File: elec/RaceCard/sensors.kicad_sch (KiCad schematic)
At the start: 0 parts

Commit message: + lib C3I_A25 et IQS7222A001QFR
ajout de IQS7222A001QFR dans le sch de sensors
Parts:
- added C1, C3, C5: 100pF, Capacitor_SMD:C_0603_1608Metric, symbol Device:C_Small
- added C2, C4: 2.2uF, Capacitor_SMD:C_0603_1608Metric, symbol Device:C_Small
- added C6: 4.7uF, Capacitor_SMD:C_0603_1608Metric, symbol Device:C_Small
- added U1: ~, symbol C3I_A25:IQS7222A001QFR
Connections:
- new net: C1.1, C2.1, U1.4 (VREGA)
- new net: C3.1, C4.1, U1.2 (VREGD)
- new net: C5.1, C6.1, U1.1 (VDD)
- new net GND: C1.2, C2.2, C3.2, C4.2, C5.2, C6.2, U1.21 (GND_TAB), U1.3 (VSS)

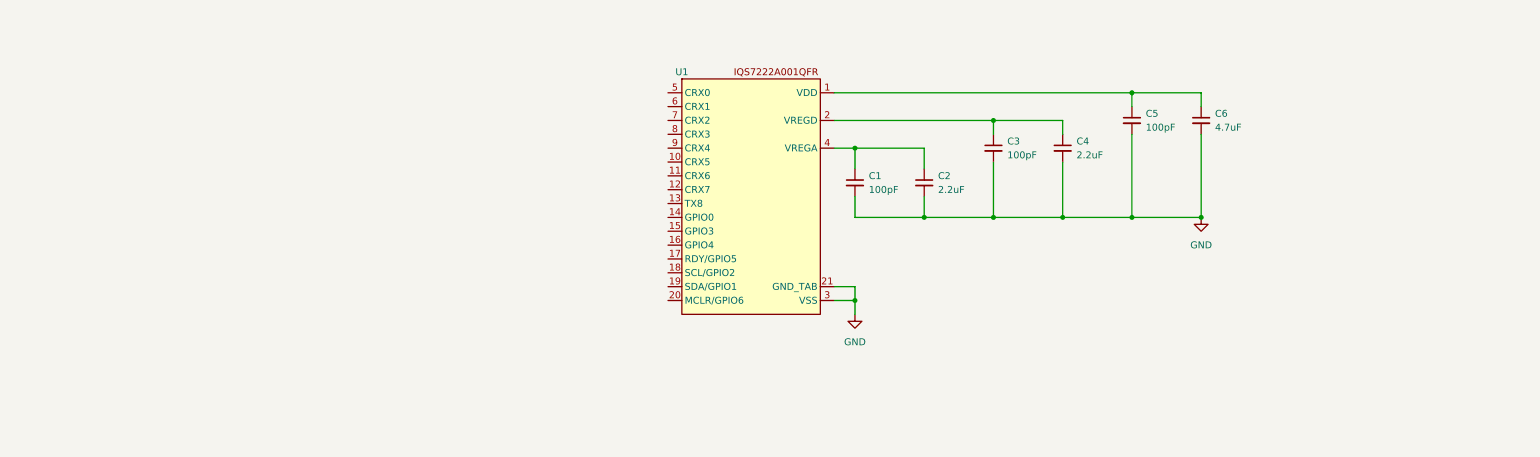
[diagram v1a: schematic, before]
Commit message: schematic slider + btns (à valider)
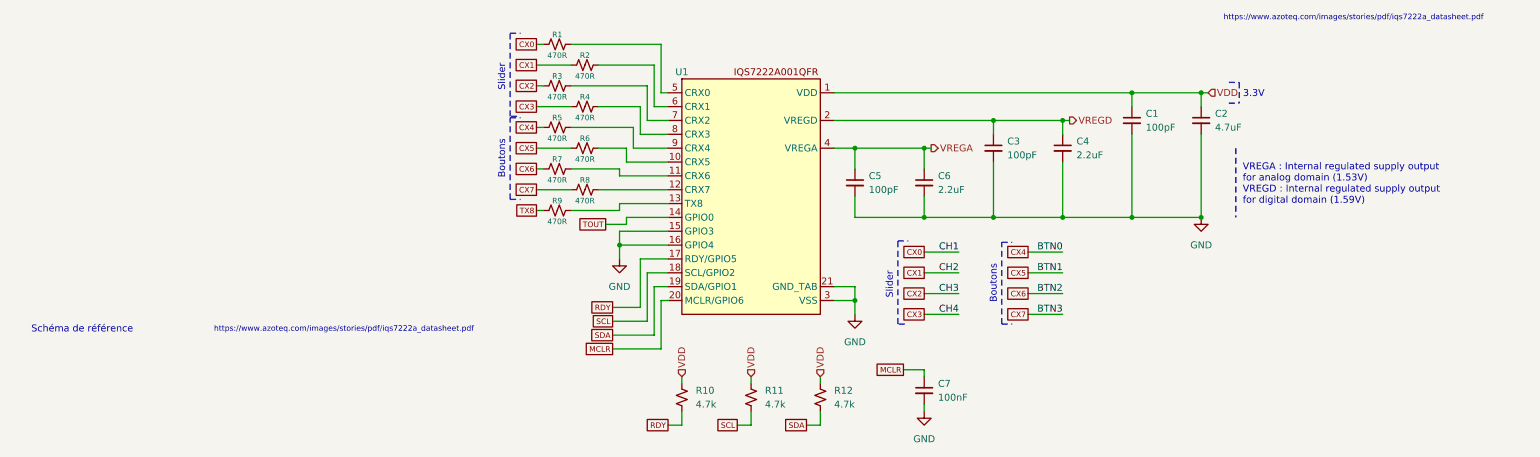
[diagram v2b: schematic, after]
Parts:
- added C7: 100nF, Capacitor_SMD:C_0603_1608Metric, symbol Device:C_Small
- added R1, R2, R3, R4, R5, R6, R7, R8, R9: 470R, Resistor_SMD:R_0603_1608Metric, symbol Device:R_Small_US
- added R10, R11, R12: 4.7k, Resistor_SMD:R_0603_1608Metric, symbol Device:R_Small_US
- U1: value ~ -> IQS7222A001QFR
- renumbered C5 to C1, C6 to C2, C1 to C5, C2 to C6
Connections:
- net GND: now also U1.15 (GPIO3), U1.16 (GPIO4), C7.2
- net VREGA: now reaches C5.1, C6.1, U1.4 (VREGA)
- net VREGD: now reaches C3.1, C4.1, U1.2 (VREGD)
- net VDD: now reaches C1.1, C2.1, U1.1 (VDD)
- net VDD: now also R10.1, R11.1, R12.1
- net at U1.10 (CRX5): now also R6.2
- net at U1.11 (CRX6): now also R7.2
- net at U1.12 (CRX7): now also R8.2
- net at U1.13 (TX8): now also R9.2
- net TOUT: now reaches U1.14 (GPIO0)
- net RDY: now reaches U1.17 (RDY/GPIO5)
- net RDY: now also R10.2
- net SCL: now reaches U1.18 (SCL/GPIO2)
- net SCL: now also R11.2
- net SDA: now reaches U1.19 (SDA/GPIO1)
- net SDA: now also R12.2
- net MCLR: now reaches U1.20 (MCLR/GPIO6)
- net MCLR: now also C7.1
- net at U1.5 (CRX0): now also R1.2
- net at U1.6 (CRX1): now also R2.2
- net at U1.7 (CRX2): now also R3.2
- net at U1.8 (CRX3): now also R4.2
- net at U1.9 (CRX4): now also R5.2
- new net CX0: R1.1
- new net CX1: R2.1
- new net CX2: R3.1
- new net CX3: R4.1
- new net CX4: R5.1
- new net CX5: R6.1
- new net CX6: R7.1
- new net CX7: R8.1
- new net TX8: R9.1
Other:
- note added: "3.3V"
- note added: "Boutons"
- note added: "Schéma de référence"
- note added: "Slider"
- note added: "VREGA : Internal regulated supply output for analog domain (1.53V) VREGD : Internal regulated supply output for digital domain (1.59V)"
- note added: "https://www.azoteq.com/images/stories/pdf/iqs7222a_datasheet.pdf"

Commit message: + test points
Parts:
- added TP2: VDD, TestPoint:TestPoint_THTPad_3.0x3.0mm_Drill1.5mm, symbol Connector:TestPoint
- renumbered C3 to C10, C4 to C11, C5 to C12, C6 to C13, C7 to C14, C1 to C8, C2 to C9, R9 to R10, R10 to R11, R11 to R12, R12 to R13, R1 to R2, R2 to R3, R3 to R4, R4 to R5, R5 to R6, R6 to R7, R7 to R8, R8 to R9, U1 to U2
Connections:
- net VDD: now also TP2.1
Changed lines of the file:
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@@
 		)
 	)
+	(wire
+		(pts
+			(xy 215.9 77.47) (xy 215.9 78.74)
+		)
+		(stroke
+			(width 0)
+			(type default)
+		)
+	)
 	(polyline
 		(pts
@@
 		(on_board yes)
 		(dnp no)
-		(property "Reference" "R6"
+		(property "Reference" "R7"
 			(at 115.57 87.122 90)
 			(effects
@@
 			(project "RaceCard"
 				(path "/fef6ab1d-cc84-41bb-aff7-8da28fd37bf7/e67e86ec-ba20-42a7-8035-4d69feadf404"
-					(reference "R6")
+					(reference "R7")
 					(unit 1)
 				)
@@
 		(dnp no)
 		(fields_autoplaced yes)
-		(property "Reference" "C5"
+		(property "Reference" "C12"
 			(at 167.64 93.9862 0)
 			(effects
@@
 			(project ""
 				(path "/fef6ab1d-cc84-41bb-aff7-8da28fd37bf7/e67e86ec-ba20-42a7-8035-4d69feadf404"
-					(reference "C5")
+					(reference "C12")
 					(unit 1)
 				)
@@
 		(dnp no)
 		(fields_autoplaced yes)
-		(property "Reference" "C4"
+		(property "Reference" "C11"
 			(at 205.74 87.6362 0)
 			(effects
@@
 			(project "RaceCard"
 				(path "/fef6ab1d-cc84-41bb-aff7-8da28fd37bf7/e67e86ec-ba20-42a7-8035-4d69feadf404"
-					(reference "C4")
+					(reference "C11")
 					(unit 1)
 				)
@@
 		(dnp no)
 		(fields_autoplaced yes)
-		(property "Reference" "C1"
+		(property "Reference" "C8"
 			(at 218.44 82.5562 0)
 			(effects
@@
 			(project "RaceCard"
 				(path "/fef6ab1d-cc84-41bb-aff7-8da28fd37bf7/e67e86ec-ba20-42a7-8035-4d69feadf404"
-					(reference "C1")
+					(reference "C8")
 					(unit 1)
 				)
@@
 		(on_board yes)
 		(dnp no)
-		(property "Reference" "R3"
+		(property "Reference" "R4"
 			(at 110.49 75.692 90)
 			(effects
@@
 			(project "RaceCard"
 				(path "/fef6ab1d-cc84-41bb-aff7-8da28fd37bf7/e67e86ec-ba20-42a7-8035-4d69feadf404"
-					(reference "R3")
+					(reference "R4")
 					(unit 1)
 				)
@@
 		(dnp no)
 		(fields_autoplaced yes)
-		(property "Reference" "R11"
+		(property "Reference" "R12"
 			(at 148.59 133.3499 0)
 			(effects
@@
 			(project "RaceCard"
 				(path "/fef6ab1d-cc84-41bb-aff7-8da28fd37bf7/e67e86ec-ba20-42a7-8035-4d69feadf404"
-					(reference "R11")
+					(reference "R12")
 					(unit 1)
 				)
@@
 		(dnp no)
 		(fields_autoplaced yes)
-		(property "Reference" "C6"
+		(property "Reference" "C13"
 			(at 180.34 93.9862 0)
 			(effects
@@
 			(project "RaceCard"
 				(path "/fef6ab1d-cc84-41bb-aff7-8da28fd37bf7/e67e86ec-ba20-42a7-8035-4d69feadf404"
-					(reference "C6")
+					(reference "C13")
 					(unit 1)
 				)
@@
 		(on_board yes)
 		(dnp no)
-		(property "Reference" "R5"
+		(property "Reference" "R6"
 			(at 110.49 83.312 90)
 			(effects
@@
 			(project "RaceCard"
 				(path "/fef6ab1d-cc84-41bb-aff7-8da28fd37bf7/e67e86ec-ba20-42a7-8035-4d69feadf404"
-					(reference "R5")
+					(reference "R6")
+					(unit 1)
+				)
+			)
+		)
+	)
+	(symbol
+		(lib_id "Connector:TestPoint")
+		(at 215.9 77.47 0)
+		(unit 1)
+		(exclude_from_sim no)
+		(in_bom yes)
+		(on_board yes)
+		(dnp no)
+		(fields_autoplaced yes)
+		(property "Reference" "TP2"
+			(at 218.44 72.8979 0)
+			(effects
+				(font
+					(size 1.27 1.27)
+				)
+				(justify left)
+			)
+		)
+		(property "Value" "VDD"
+			(at 218.44 75.4379 0)
+			(effects
+				(font
+					(size 1.27 1.27)
+				)
+				(justify left)
+			)
+		)
+		(property "Footprint" "TestPoint:TestPoint_THTPad_3.0x3.0mm_Drill1.5mm"
+			(at 220.98 77.47 0)
+			(effects
+				(font
+					(size 1.27 1.27)
+				)
+				(hide yes)
+			)
+		)
+		(property "Datasheet" "~"
+			(at 220.98 77.47 0)
+			(effects
+				(font
+					(size 1.27 1.27)
+				)
+				(hide yes)
+			)
+		)
+		(property "Description" "test point"
+			(at 215.9 77.47 0)
+			(effects
+				(font
+					(size 1.27 1.27)
+				)
+				(hide yes)
+			)
+		)
+		(pin "1"
+		)
+		(instances
+			(project "RaceCard"
+				(path "/fef6ab1d-cc84-41bb-aff7-8da28fd37bf7/e67e86ec-ba20-42a7-8035-4d69feadf404"
+					(reference "TP2")
 					(unit 1)
 				)
@@
 		(on_board yes)
 		(dnp no)
-		(property "Reference" "R4"
+		(property "Reference" "R5"
 			(at 115.57 79.502 90)
 			(effects
@@
 			(project ""
 				(path "/fef6ab1d-cc84-41bb-aff7-8da28fd37bf7/e67e86ec-ba20-42a7-8035-4d69feadf404"
-					(reference "R4")
+					(reference "R5")
 					(unit 1)
 				)
@@
 		(on_board yes)
 		(dnp no)
-		(property "Reference" "R7"
+		(property "Reference" "R8"
 			(at 110.49 90.932 90)
 			(effects
@@
 			(project "RaceCard"
 				(path "/fef6ab1d-cc84-41bb-aff7-8da28fd37bf7/e67e86ec-ba20-42a7-8035-4d69feadf404"
-					(reference "R7")
+					(reference "R8")
 					(unit 1)
 				)
@@
 		(on_board yes)
 		(dnp no)
-		(property "Reference" "R1"
+		(property "Reference" "R2"
 			(at 110.49 68.072 90)
 			(effects
@@
 			(project "RaceCard"
 				(path "/fef6ab1d-cc84-41bb-aff7-8da28fd37bf7/e67e86ec-ba20-42a7-8035-4d69feadf404"
-					(reference "R1")
+					(reference "R2")
 					(unit 1)
 				)
@@
 		(dnp no)
 		(fields_autoplaced yes)
-		(property "Reference" "R10"
+		(property "Reference" "R11"
 			(at 135.89 133.3499 0)
 			(effects
@@
 			(project ""
 				(path "/fef6ab1d-cc84-41bb-aff7-8da28fd37bf7/e67e86ec-ba20-42a7-8035-4d69feadf404"
-					(reference "R10")
+					(reference "R11")
 					(unit 1)
 				)
@@
 		(dnp no)
 		(fields_autoplaced yes)
-		(property "Reference" "R12"
+		(property "Reference" "R13"
 			(at 161.29 133.3499 0)
 			(effects
@@
 			(project "RaceCard"
 				(path "/fef6ab1d-cc84-41bb-aff7-8da28fd37bf7/e67e86ec-ba20-42a7-8035-4d69feadf404"
-					(reference "R12")
+					(reference "R13")
 					(unit 1)
 				)
@@
 		(dnp no)
 		(fields_autoplaced yes)
-		(property "Reference" "C3"
+		(property "Reference" "C10"
 			(at 193.04 87.6362 0)
 			(effects
@@
 			(project "RaceCard"
 				(path "/fef6ab1d-cc84-41bb-aff7-8da28fd37bf7/e67e86ec-ba20-42a7-8035-4d69feadf404"
-					(reference "C3")
+					(reference "C10")
 					(unit 1)
 				)
@@
 		(dnp no)
 		(fields_autoplaced yes)
-		(property "Reference" "C7"
+		(property "Reference" "C14"
 			(at 180.34 132.0862 0)
 			(effects
@@
 			(project "RaceCard"
 				(path "/fef6ab1d-cc84-41bb-aff7-8da28fd37bf7/e67e86ec-ba20-42a7-8035-4d69feadf404"
-					(reference "C7")
+					(reference "C14")
 					(unit 1)
 				)
@@
 		(on_board yes)
 		(dnp no)
-		(property "Reference" "R8"
+		(property "Reference" "R9"
 			(at 115.57 94.742 90)
 			(effects
@@
 			(project "RaceCard"
 				(path "/fef6ab1d-cc84-41bb-aff7-8da28fd37bf7/e67e86ec-ba20-42a7-8035-4d69feadf404"
-					(reference "R8")
+					(reference "R9")
 					(unit 1)
 				)
@@
 		(dnp no)
 		(fields_autoplaced yes)
-		(property "Reference" "C2"
+		(property "Reference" "C9"
 			(at 231.14 82.5562 0)
 			(effects
@@
 			(project "RaceCard"
 				(path "/fef6ab1d-cc84-41bb-aff7-8da28fd37bf7/e67e86ec-ba20-42a7-8035-4d69feadf404"
-					(reference "C2")
+					(reference "C9")
 					(unit 1)
 				)
@@
 		(dnp no)
 		(fields_autoplaced yes)
-		(property "Reference" "U1"
+		(property "Reference" "U2"
 			(at 133.35 74.93 0)
 			(do_not_autoplace yes)
@@
 			(project ""
 				(path "/fef6ab1d-cc84-41bb-aff7-8da28fd37bf7/e67e86ec-ba20-42a7-8035-4d69feadf404"
-					(reference "U1")
+					(reference "U2")
 					(unit 1)
 				)
@@
 		(on_board yes)
 		(dnp no)
-		(property "Reference" "R2"
+		(property "Reference" "R3"
 			(at 115.57 71.882 90)
 			(effects
@@
 			(project "RaceCard"
 				(path "/fef6ab1d-cc84-41bb-aff7-8da28fd37bf7/e67e86ec-ba20-42a7-8035-4d69feadf404"
-					(reference "R2")
+					(reference "R3")
 					(unit 1)
 				)
@@
 		(on_board yes)
 		(dnp no)
-		(property "Reference" "R9"
+		(property "Reference" "R10"
 			(at 110.49 98.552 90)
 			(effects
@@
 			(project "RaceCard"
 				(path "/fef6ab1d-cc84-41bb-aff7-8da28fd37bf7/e67e86ec-ba20-42a7-8035-4d69feadf404"
-					(reference "R9")
+					(reference "R10")
 					(unit 1)
 				)

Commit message: Fix des footprints et edge cuts
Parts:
- removed R9: 470R, Resistor_SMD:R_0603_1608Metric, symbol Device:R_Small_US
- added TP11: TOUT, TestPoint:TestPoint_THTPad_3.0x3.0mm_Drill1.5mm, symbol Connector:TestPoint
- U2: footprint (none) -> C3I_A25:IQS7222A001CSR
- renumbered R11 to R10, R12 to R11, R13 to R12, R10 to R9, TP2 to TP10
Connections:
- net CX4 is gone; now on net CX5: R6.1
- net CX5: no longer R7.1
- net CX6: now also R7.1; no longer R8.1
- net CX7: now also R8.1
- net GND: now also U2.B2 (GPIO4), U2.D4 (VSS); no longer U2.15 (GPIO3), U2.16 (GPIO4), U2.21 (GND_TAB), U2.3 (VSS)
- net MCLR: now also U2.A5 (MCLR/GPIO6); no longer U2.20 (MCLR/GPIO6)
- net RDY: now also U2.C3 (RDY/GPIO5); no longer U2.17 (RDY/GPIO5)
- net SCL: now also U2.A3 (SCL/GPIO2); no longer U2.18 (SCL/GPIO2)
- net SDA: now also U2.B4 (SDA/GPIO1); no longer U2.19 (SDA/GPIO1)
- net VDD: now also U2.C5 (VDD); no longer U2.1 (VDD)
- net VREGA: now also U2.G5 (VREGA); no longer U2.4 (VREGA)
- net VREGD: now also U2.E5 (VREGD); no longer U2.2 (VREGD)
- net at R7.2: now also U2.E1 (CRX6); no longer U2.10 (CRX5)
- net at R4.2: now also U2.D2 (CRX2); no longer U2.7 (CRX2)
- net at R6.2: now also U2.F2 (CRX5); no longer U2.9 (CRX4)
- net at R5.2: now also U2.G3 (CRX3); no longer U2.8 (CRX3)
- net at R8.2: now also U2.G1 (CRX7); no longer U2.11 (CRX6)
- net at R2.2: now also U2.F4 (CRX0); no longer U2.5 (CRX0)
- net at R9.2: now also U2.C1 (TX8); no longer U2.13 (TX8)
- net at R3.2: now also U2.E3 (CRX1); no longer U2.6 (CRX1)
- removed net TOUT: U2.14 (GPIO0)
- new net: TP11.1, U2.A1 (GPIO0/GPIO3)
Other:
- moved on the sheet: R6, R7, R8

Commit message: Tout le power est routed
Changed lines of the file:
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@@
-	)
-	(junction
-		(at 165.1 116.84)
-		(diameter 0)
-		(color 0 0 0 0)
 	)
 	(junction
@@
 	(wire
 		(pts
-			(xy 165.1 114.3) (xy 165.1 116.84)
-		)
-		(stroke
-			(width 0)
-			(type default)
-		)
-	)
-	(wire
-		(pts
 			(xy 130.81 81.28) (xy 128.27 81.28)
 		)
@@
 		)
 	)
-	(wire
-		(pts
-			(xy 161.29 114.3) (xy 165.1 114.3)
-		)
-		(stroke
-			(width 0)
-			(type default)
-		)
-	)
